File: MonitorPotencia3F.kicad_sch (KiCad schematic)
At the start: 30 parts, among them J1 Conn_01x02, J2 Conn_01x02, J3 Conn_01x02, J4 Conn_01x02, J5 Conn_01x02, J6 Conn_01x04, J7 Conn_01x04, J8 Conn_01x04, J9 Conn_02x09_Odd_Even, U1 LM7805, U2 ESP32-DEVKIT-V1, U3 LM324

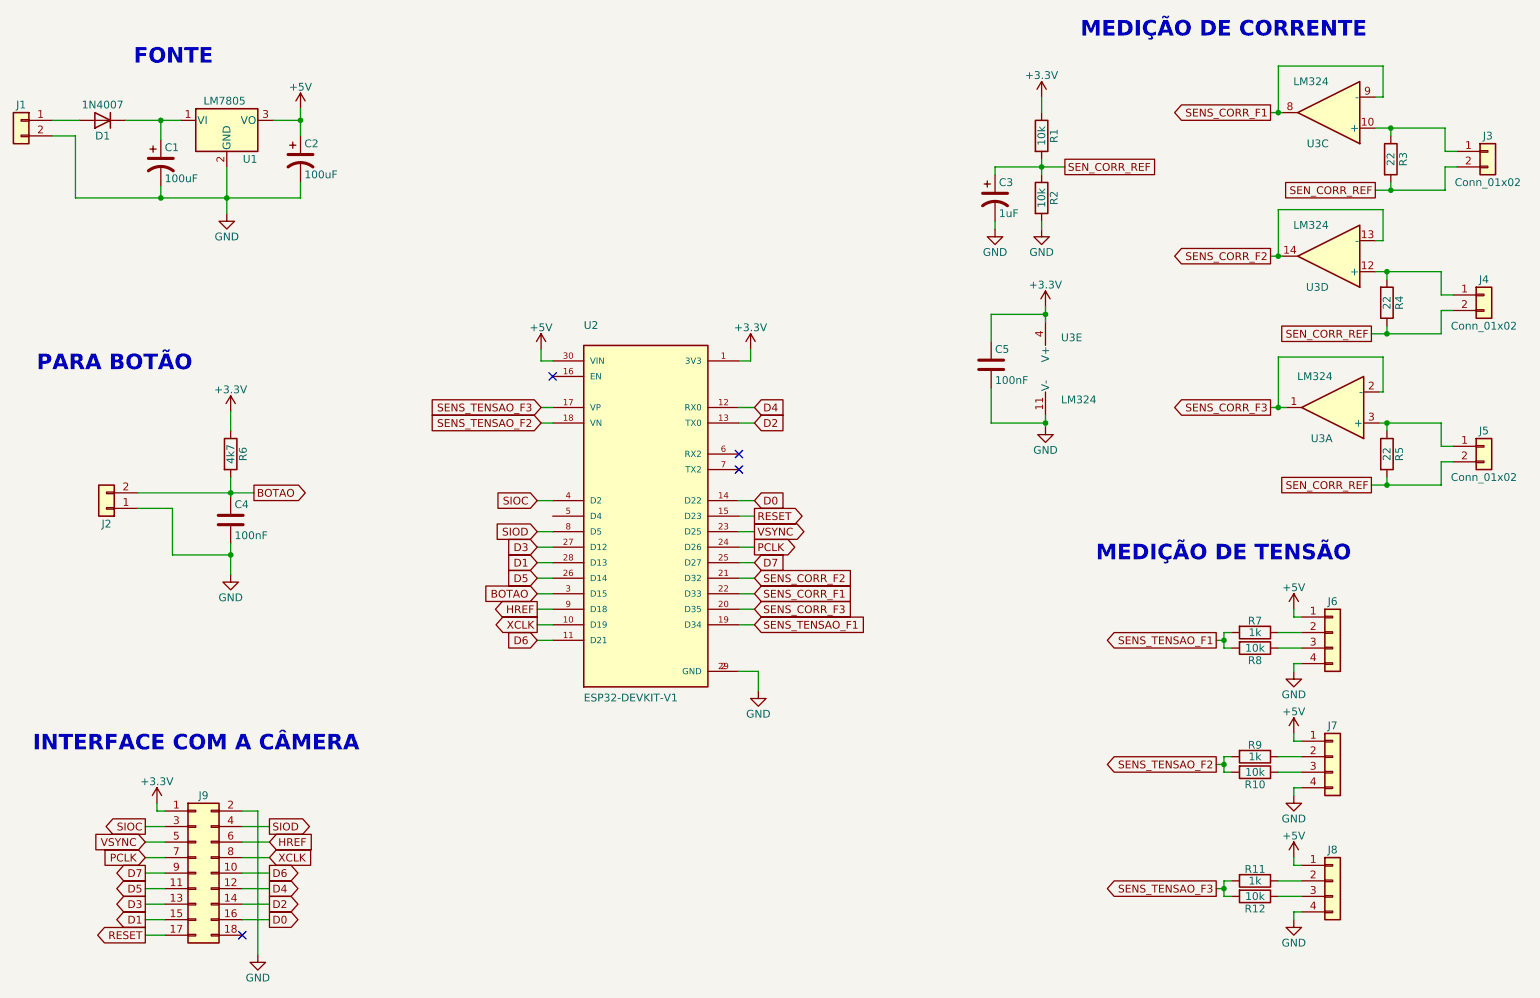
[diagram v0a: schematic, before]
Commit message: Atualização do projeto com novos sensores de tensão. A referência de tensão para os sensores de corrente também foi atualizada, incluindo um buffer para isolação do divisor de tensão. Os Footprints também foram atualizados para a nova versão do KiCad, a versão 6.0
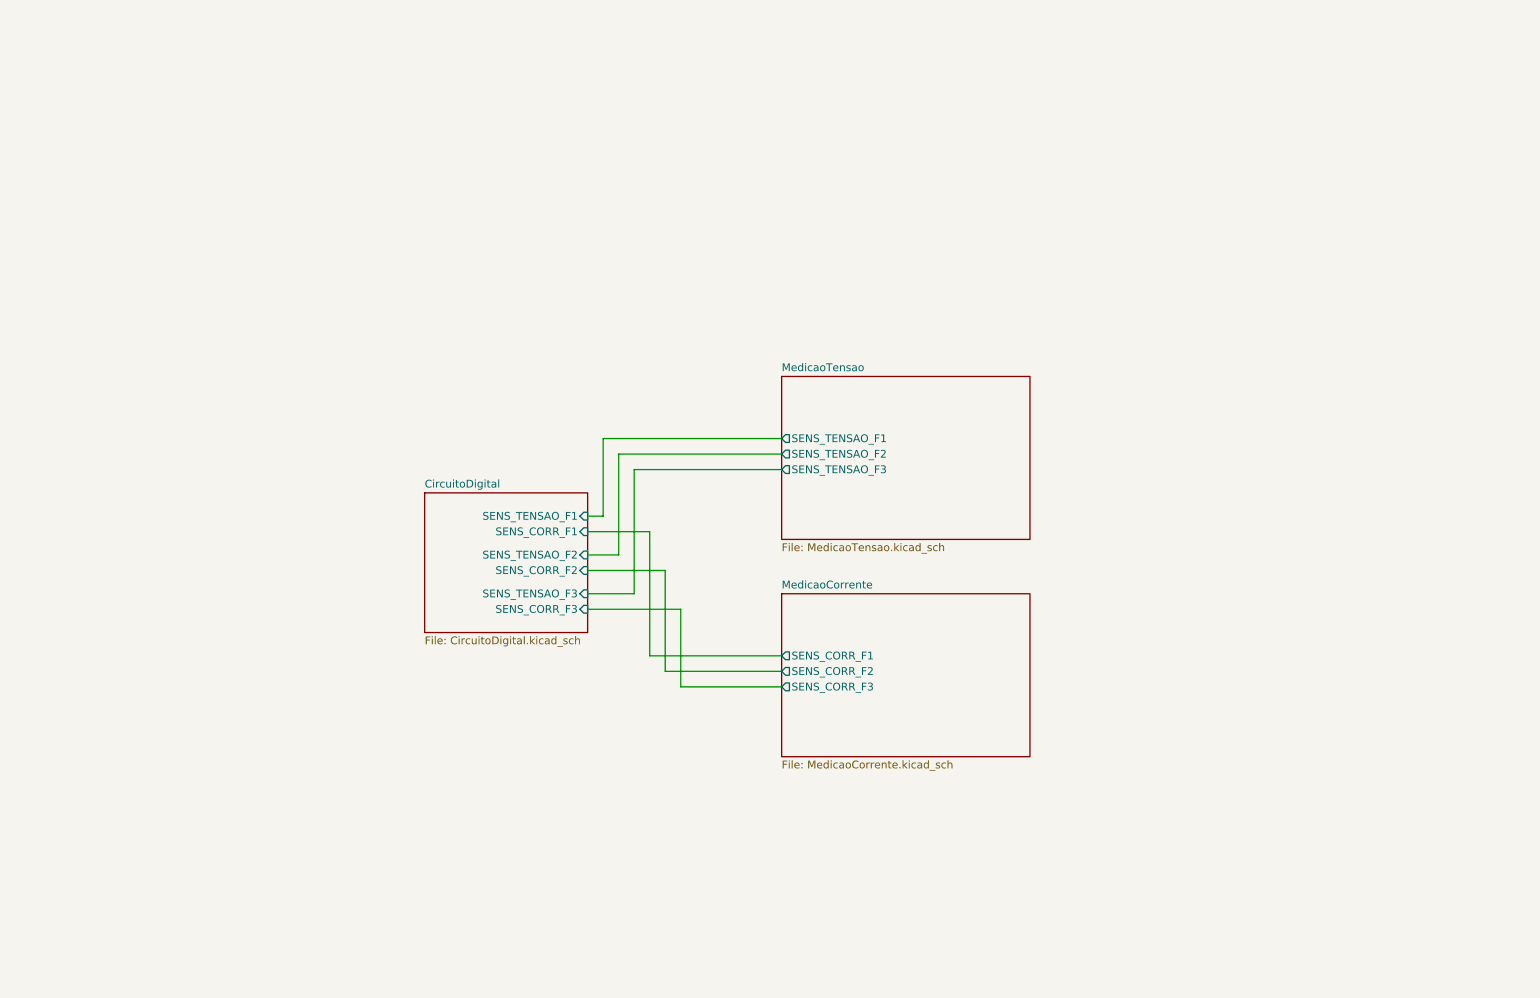
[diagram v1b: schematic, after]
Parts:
- removed C1, C2: 100uF, Capacitors_THT:CP_Radial_D6.3mm_P2.50mm, symbol Device:CP1
- removed C3: 1uF, Capacitors_THT:CP_Radial_D6.3mm_P2.50mm, symbol Device:CP1
- removed C4, C5: 100nF, Capacitors_THT:C_Rect_L7.0mm_W2.0mm_P5.00mm, symbol Device:C
- removed D1: 1N4007, Diodes_THT:D_DO-41_SOD81_P10.16mm_Horizontal, symbol Diode:1N4007
- removed J1, J2, J3, J4, J5: Conn_01x02, Connectors_Terminal_Blocks:TerminalBlock_bornier-2_P5.08mm, symbol Connector_Generic:Conn_01x02
- removed J6, J7, J8: Conn_01x04, Connectors_Terminal_Blocks:TerminalBlock_bornier-4_P5.08mm, symbol Connector_Generic:Conn_01x04
- removed J9: Conn_02x09_Odd_Even, Pin_Headers:Pin_Header_Straight_2x09_Pitch2.54mm, symbol Connector_Generic:Conn_02x09_Odd_Even
- removed R1, R10, R12, R2, R8: 10k, Resistors_THT:R_Axial_DIN0207_L6.3mm_D2.5mm_P10.16mm_Horizontal, symbol Device:R
- removed R11, R7, R9: 1k, Resistors_THT:R_Axial_DIN0207_L6.3mm_D2.5mm_P10.16mm_Horizontal, symbol Device:R
- removed R3, R4, R5: 22, Resistors_THT:R_Axial_DIN0207_L6.3mm_D2.5mm_P10.16mm_Horizontal, symbol Device:R
- removed R6: 4k7, Resistors_THT:R_Axial_DIN0207_L6.3mm_D2.5mm_P10.16mm_Horizontal, symbol Device:R
- removed U1: LM7805, TO_SOT_Packages_THT:TO-220-3_Vertical, symbol Regulator_Linear:LM7805_TO220
- removed U2: ESP32-DEVKIT-V1, ESP32-DEVKIT-V1:MODULE_ESP32_DEVKIT_V1, symbol ESP32-DEVKIT-V1:ESP32-DEVKIT-V1
- removed U3: LM324, Housings_DIP:DIP-14_W7.62mm, symbol Amplifier_Operational:LM324
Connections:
- no-connect marks 4 -> 0
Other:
- added sheet CircuitoDigital (CircuitoDigital.kicad_sch)
- added sheet MedicaoCorrente (MedicaoCorrente.kicad_sch)
- added sheet MedicaoTensao (MedicaoTensao.kicad_sch)
- note removed: "FONTE"
- note removed: "INTERFACE COM A CÂMERA"
- note removed: "MEDIÇÃO DE CORRENTE"
- note removed: "MEDIÇÃO DE TENSÃO"
- note removed: "PARA BOTÃO"

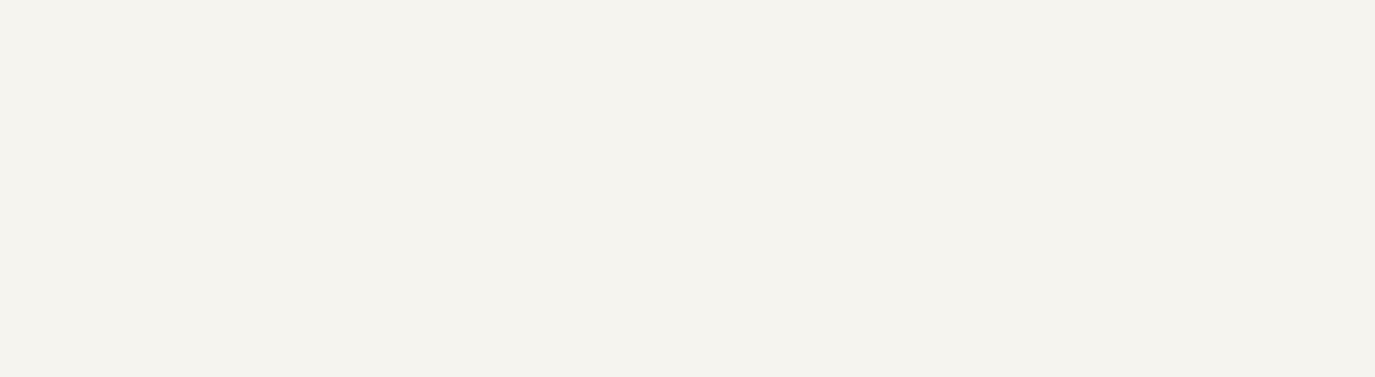
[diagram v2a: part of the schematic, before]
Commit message: Adicionado zeners de proteção para a saída dos buffers
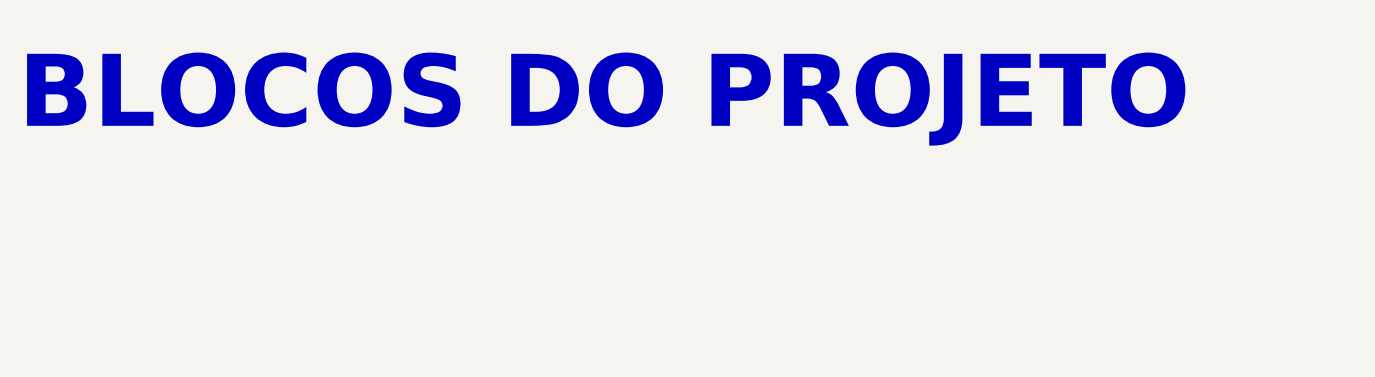
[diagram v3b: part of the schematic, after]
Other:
- note added: "BLOCOS DO PROJETO"
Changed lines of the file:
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@@
     (stroke (width 0) (type default) (color 0 0 0 0))
+  )
+  (text "BLOCOS DO PROJETO" (at 85.09 39.37 0)
+    (effects (font (size 8 8) (thickness 1.6) bold) (justify left bottom))
   )
   (sheet (at 93.98 96.52) (size 26.67 22.86) (fields_autoplaced)
@@
       (reference "#PWR019") (unit 1) (value "GND") (footprint "")
     )
+    (path "/1418463a-4889-46ec-a4c0-cb865c532c6c/9b5bd37c-524b-4116-83e7-da55a5bde93e"
+      (reference "#PWR020") (unit 1) (value "GND") (footprint "")
+    )
+    (path "/1418463a-4889-46ec-a4c0-cb865c532c6c/2d8909e6-b573-41e7-96c6-2cf61ea0a08b"
+      (reference "#PWR021") (unit 1) (value "GND") (footprint "")
+    )
+    (path "/1418463a-4889-46ec-a4c0-cb865c532c6c/4df2cb7c-5a01-4651-b4f3-e48445a80da6"
+      (reference "#PWR022") (unit 1) (value "GND") (footprint "")
+    )
     (path "/0fd56df2-b828-4ab9-b5a9-d7782f3e0762/7fc1edd1-3027-4691-872c-de9ccb441181"
-      (reference "#PWR?") (unit 1) (value "+3.3V") (footprint "")
+      (reference "#PWR023") (unit 1) (value "+3.3V") (footprint "")
     )
     (path "/0fd56df2-b828-4ab9-b5a9-d7782f3e0762/cd4e2187-9a56-4be6-8ba6-fe72381b453c"
-      (reference "#PWR?") (unit 1) (value "GND") (footprint "")
+      (reference "#PWR024") (unit 1) (value "GND") (footprint "")
+    )
+    (path "/93340c38-8bfd-447a-bf60-be3c6dc860d9/72394d4a-0f52-4277-bc9a-622c82eea96f"
+      (reference "#PWR025") (unit 1) (value "GND") (footprint "")
+    )
+    (path "/93340c38-8bfd-447a-bf60-be3c6dc860d9/ad73368f-624d-4e30-b7ab-e4add3ccd24c"
+      (reference "#PWR026") (unit 1) (value "GND") (footprint "")
+    )
+    (path "/93340c38-8bfd-447a-bf60-be3c6dc860d9/5a76d035-f48c-4447-b365-8c77039e0390"
+      (reference "#PWR027") (unit 1) (value "GND") (footprint "")
     )
     (path "/93340c38-8bfd-447a-bf60-be3c6dc860d9/b57488f4-373a-4e8c-a509-bd6f3b44b399"
@@
       (reference "D1") (unit 1) (value "1N4007") (footprint "Diode_THT:D_DO-41_SOD81_P10.16mm_Horizontal")
     )
+    (path "/1418463a-4889-46ec-a4c0-cb865c532c6c/e6a1a139-219b-49eb-94b4-9e1f23014712"
+      (reference "D2") (unit 1) (value "1N4728A") (footprint "Diode_THT:D_DO-41_SOD81_P10.16mm_Horizontal")
+    )
+    (path "/1418463a-4889-46ec-a4c0-cb865c532c6c/17abb941-9b93-489c-8535-d503df97c109"
+      (reference "D3") (unit 1) (value "1N4728A") (footprint "Diode_THT:D_DO-41_SOD81_P10.16mm_Horizontal")
+    )
+    (path "/1418463a-4889-46ec-a4c0-cb865c532c6c/7de3092c-e71e-439a-8a91-3360afd00de6"
+      (reference "D4") (unit 1) (value "1N4728A") (footprint "Diode_THT:D_DO-41_SOD81_P10.16mm_Horizontal")
+    )
+    (path "/93340c38-8bfd-447a-bf60-be3c6dc860d9/5b230479-1b8b-4509-8f66-e21f89466816"
+      (reference "D5") (unit 1) (value "1N4728A") (footprint "Diode_THT:D_DO-41_SOD81_P10.16mm_Horizontal")
+    )
+    (path "/93340c38-8bfd-447a-bf60-be3c6dc860d9/3f735eff-1e2f-4130-88b7-646cb7bcb199"
+      (reference "D6") (unit 1) (value "1N4728A") (footprint "Diode_THT:D_DO-41_SOD81_P10.16mm_Horizontal")
+    )
+    (path "/93340c38-8bfd-447a-bf60-be3c6dc860d9/511325e4-8c68-49eb-913c-32b0583fba6c"
+      (reference "D7") (unit 1) (value "1N4728A") (footprint "Diode_THT:D_DO-41_SOD81_P10.16mm_Horizontal")
+    )
     (path "/93340c38-8bfd-447a-bf60-be3c6dc860d9/e6172b77-d4be-4920-b4d0-361b1247b45e"
